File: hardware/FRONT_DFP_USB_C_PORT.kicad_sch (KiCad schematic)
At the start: 31 parts, among them J8 USB4200-03-A (VIRT FLAG MOUNT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, Q22 PMPB09R5VPX, Q23 PMPB09R5VPX, Q24 PMPB09R5VPX, Q25 PMPB09R5VPX, U13 USB5926C, U16 PTN5100BMSP

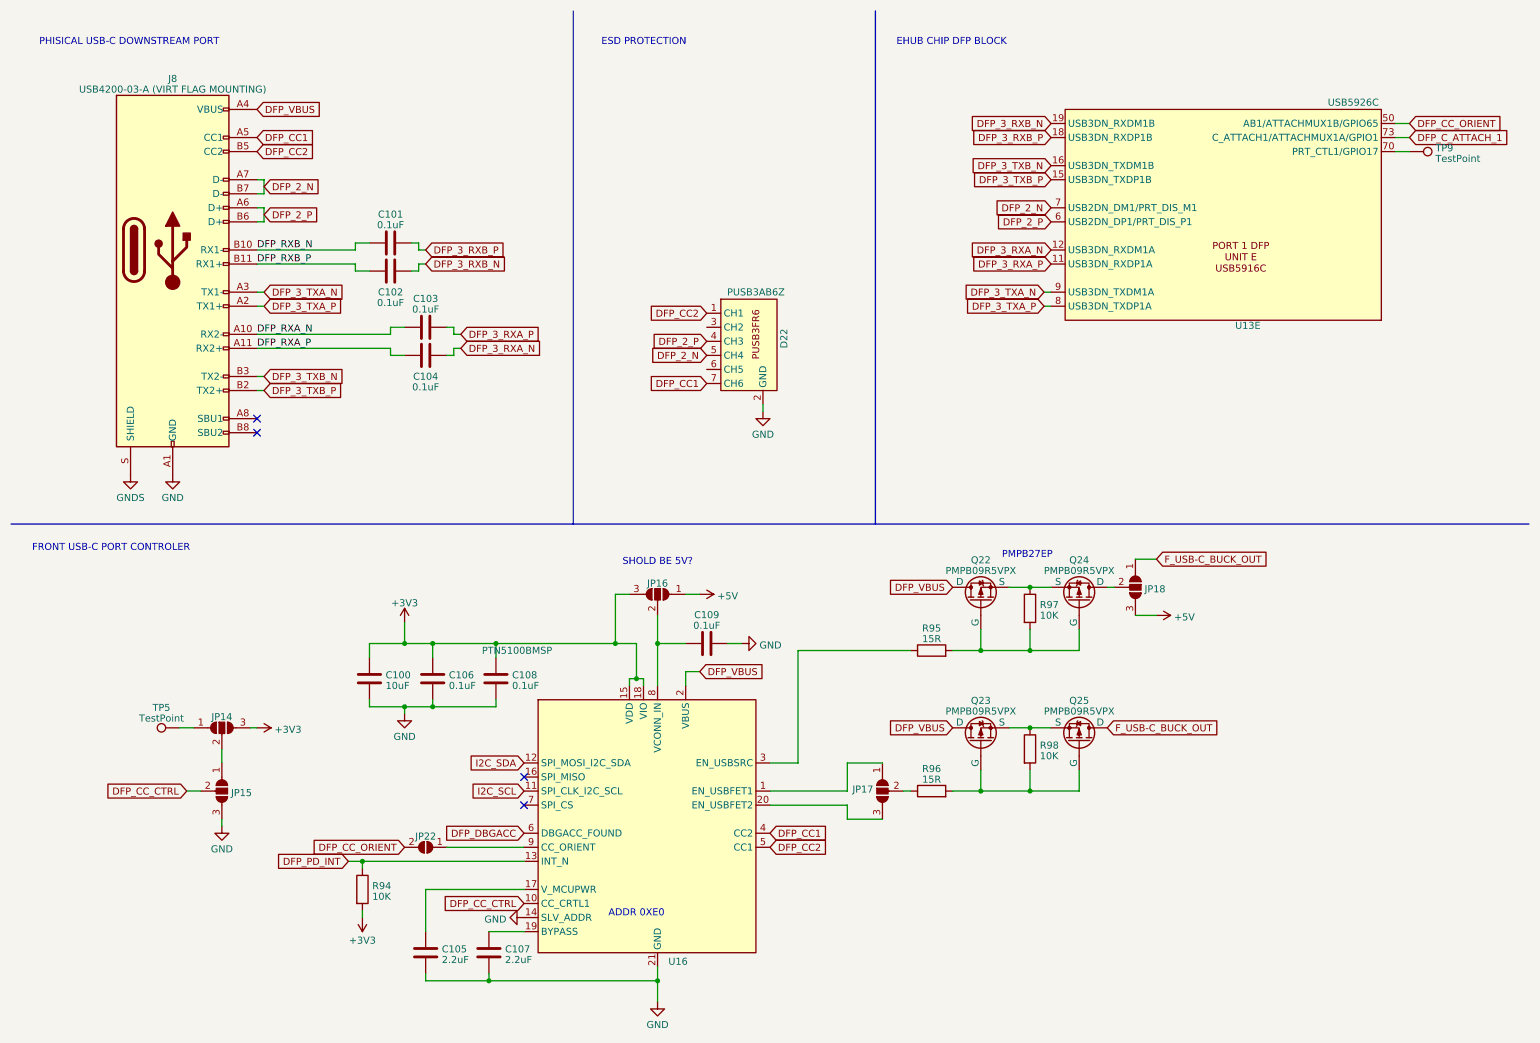
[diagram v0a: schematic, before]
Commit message: switched pd phy as old one needed an NDA
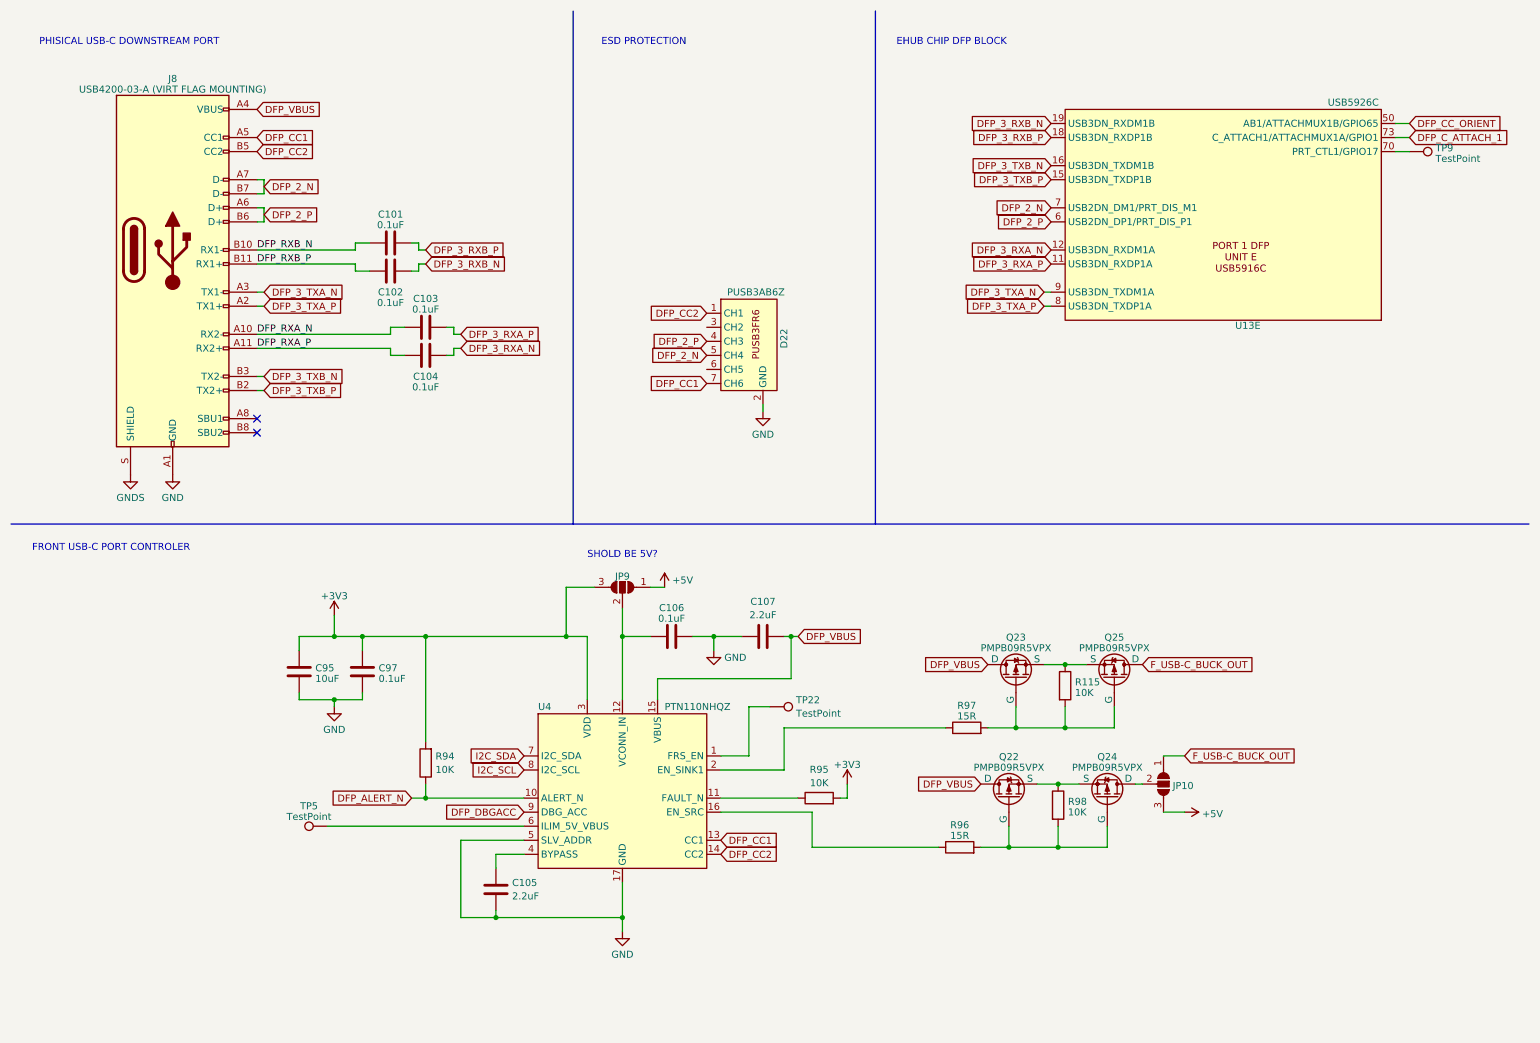
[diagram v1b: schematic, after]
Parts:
- removed C100: 10uF, Capacitor_SMD:C_0603_1608Metric, symbol Device:C
- removed C108, C109: 0.1uF, Capacitor_SMD:C_0603_1608Metric, symbol Device:C
- removed JP14, JP15, JP16, JP17, JP18: ~, Jumper:SolderJumper-3_P1.3mm_Open_RoundedPad1.0x1.5mm_NumberLabels, symbol Jumper:SolderJumper_3_Open
- removed JP22: ~, Jumper:SolderJumper-2_P1.3mm_Open_RoundedPad1.0x1.5mm, symbol Jumper:SolderJumper_2_Open
- removed U16: PTN5100BMSP, CARTHING:PTN5100BSMP, symbol CARTHING:PTN5100
- added C95: 10uF, Capacitor_SMD:C_0603_1608Metric, symbol Device:C
- added C97: 0.1uF, Capacitor_SMD:C_0603_1608Metric, symbol Device:C
- added JP10, JP9: ~, Jumper:SolderJumper-3_P1.3mm_Open_RoundedPad1.0x1.5mm_NumberLabels, symbol Jumper:SolderJumper_3_Open
- added R115: 10K, Resistor_SMD:R_0603_1608Metric, symbol Device:R
- added TP22: TestPoint, TestPoint:TestPoint_Pad_D1.5mm, symbol Connector:TestPoint
- added U4: PTN110NHQZ, CARTHING:PTN110, symbol CARTHING:PTN110
- R95: value 15R -> 10K
- R97: value 10K -> 15R
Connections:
- net +3V3: now also R95.2, C95.1, C97.1, JP9.3 (B), U4.3 (VDD); no longer C106.1
- net +5V: now also JP10.3 (B), JP9.1 (A)
- net DFP_CC1: now also U4.13 (CC1)
- net DFP_CC2: now also U4.14 (CC2)
- net DFP_DBGACC: now also U4.9 (DBG_ACC)
- net DFP_VBUS: now also C107.2, U4.15 (VBUS)
- net F_USB-C_BUCK_OUT: now also JP10.1 (A)
- net GND: now also C107.1, C95.2, C97.2, U4.17 (GND), U4.5 (SLV_ADDR); no longer C107.2
- net I2C_SCL: now also U4.8 (I2C_SCL)
- net I2C_SDA: now also U4.7 (I2C_SDA)
- net at Q23.4 (S), Q23.8 (S), Q25.4 (S)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: now also R115.1; no longer R98.1
- net at Q23.3 (G), Q25.3 (G): now also R97.2, R115.2; no longer R96.2, R98.2
- net at Q24.1 (D), Q24.2 (D), Q24.5 (D)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: now also JP10.2 (C)
- net at Q22.3 (G), Q24.3 (G): now also R96.2, R98.2; no longer R95.2, R97.2
- net at Q22.4 (S), Q22.8 (S), Q24.4 (S)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: now also R98.1; no longer R97.1
- net at R95.1: now also U4.11 (FAULT_N)
- net at R96.1: now also U4.16 (EN_SRC)
- net at C105.1: now also U4.4 (BYPASS)
- net at TP5.1: now also U4.6 (ILIM_5V_VBUS)
- net DFP_PD_INT renamed DFP_ALERT_N
- net DFP_ALERT_N: now also U4.10 (ALERT_N)
- new net: TP22.1, U4.1 (FRS_EN)
- new net: C106.1, JP9.2 (C), U4.12 (VCONN_IN)
- new net: R97.1, U4.2 (EN_SINK1)
- no-connect marks 4 -> 2
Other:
- note removed: "ADDR 0XE0"
- note removed: "PMPB27EP"

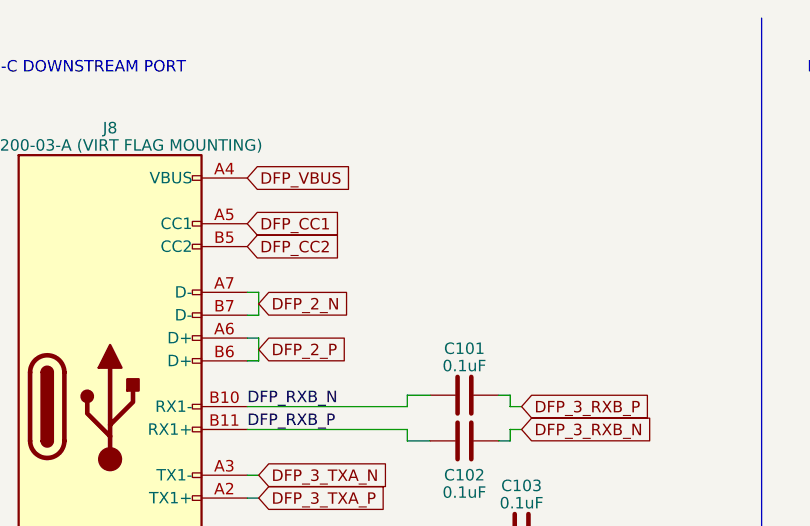
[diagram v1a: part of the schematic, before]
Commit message: updated block digram minor pcb changes
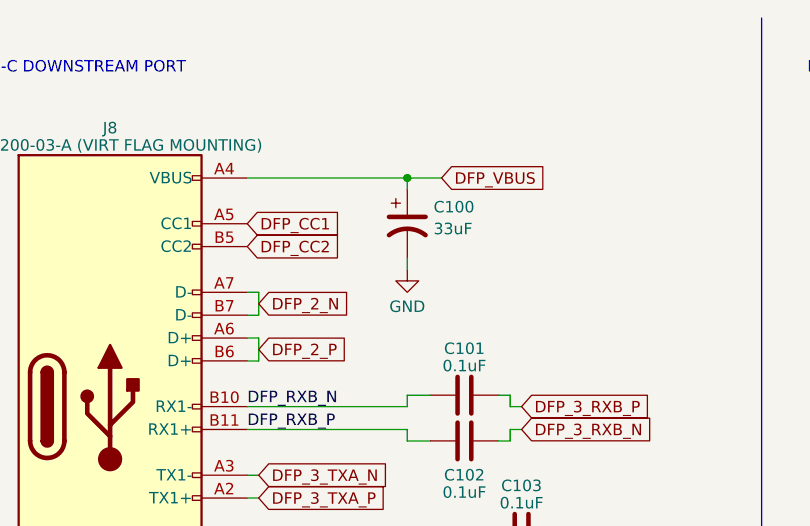
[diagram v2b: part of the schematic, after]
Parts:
- added C100: 33uF, Capacitor_SMD:C_Elec_6.3x5.8, symbol Device:C_Polarized_US
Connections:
- net DFP_VBUS: now also C100.1
- net GND: now also C100.2

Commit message: switched can tranceiver to combo controler and tranceiver
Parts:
- added TP29, TP30: TestPoint, TestPoint:TestPoint_Pad_D1.0mm, symbol Connector:TestPoint
- TP22, TP5, TP9: footprint TestPoint:TestPoint_Pad_D1.5mm -> TestPoint:TestPoint_Pad_D1.0mm
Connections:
- net at R96.1, U4.16 (EN_SRC): now also TP30.1
- net at R97.1, U4.2 (EN_SINK1): now also TP29.1
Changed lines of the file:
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@@
 	)
 	(junction
+		(at 166.37 140.97)
+		(diameter 0)
+		(color 0 0 0 0)
+	)
+	(junction
 		(at 121.92 175.26)
 		(diameter 0)
@@
 	)
 	(junction
+		(at 166.37 162.56)
+		(diameter 0)
+		(color 0 0 0 0)
+	)
+	(junction
 		(at 69.85 135.89)
 		(diameter 0)
@@
 	(wire
 		(pts
+			(xy 166.37 140.97) (xy 180.34 140.97)
+		)
+		(stroke
+			(width 0)
+			(type default)
+		)
+	)
+	(wire
+		(pts
 			(xy 99.06 173.99) (xy 99.06 175.26)
 		)
@@
 	(wire
 		(pts
-			(xy 151.13 140.97) (xy 180.34 140.97)
+			(xy 151.13 140.97) (xy 166.37 140.97)
 		)
 		(stroke
@@
 	(wire
 		(pts
+			(xy 166.37 162.56) (xy 179.07 162.56)
+		)
+		(stroke
+			(width 0)
+			(type default)
+		)
+	)
+	(wire
+		(pts
 			(xy 219.71 146.05) (xy 223.52 146.05)
 		)
@@
 	(wire
 		(pts
-			(xy 156.21 162.56) (xy 179.07 162.56)
+			(xy 156.21 162.56) (xy 166.37 162.56)
 		)
 		(stroke
@@
 			)
 		)
-		(property "Footprint" "TestPoint:TestPoint_Pad_D1.5mm"
+		(property "Footprint" "TestPoint:TestPoint_Pad_D1.0mm"
 			(at 264.16 41.91 0)
 			(effects
@@
 	)
 	(symbol
+		(lib_id "Connector:TestPoint")
+		(at 166.37 162.56 0)
+		(unit 1)
+		(exclude_from_sim no)
+		(in_bom yes)
+		(on_board yes)
+		(dnp no)
+		(fields_autoplaced yes)
+		(property "Reference" "TP30"
+			(at 167.767 158.0458 0)
+			(effects
+				(font
+					(size 1.27 1.27)
+				)
+				(justify left)
+			)
+		)
+		(property "Value" "TestPoint"
+			(at 167.767 160.4701 0)
+			(effects
+				(font
+					(size 1.27 1.27)
+				)
+				(justify left)
+			)
+		)
+		(property "Footprint" "TestPoint:TestPoint_Pad_D1.0mm"
+			(at 171.45 162.56 0)
+			(effects
+				(font
+					(size 1.27 1.27)
+				)
+				(hide yes)
+			)
+		)
+		(property "Datasheet" "~"
+			(at 171.45 162.56 0)
+			(effects
+				(font
+					(size 1.27 1.27)
+				)
+				(hide yes)
+			)
+		)
+		(property "Description" "test point"
+			(at 166.37 162.56 0)
+			(effects
+				(font
+					(size 1.27 1.27)
+				)
+				(hide yes)
+			)
+		)
+		(pin "1"
+		)
+		(instances
+			(project "usbc-car-module"
+				(path "/fae025e9-99c5-40c1-af6f-99dc1edbfa43/ad0dde3f-c33d-40ce-8876-17a95cda421b"
+					(reference "TP30")
+					(unit 1)
+				)
+			)
+		)
+	)
+	(symbol
 		(lib_id "Device:C")
 		(at 74.93 130.81 0)
@@
 			)
 		)
-		(property "Footprint" "TestPoint:TestPoint_Pad_D1.5mm"
+		(property "Footprint" "TestPoint:TestPoint_Pad_D1.0mm"
 			(at 68.58 153.67 0)
 			(effects
@@
 			)
 		)
-		(property "Footprint" "TestPoint:TestPoint_Pad_D1.5mm"
+		(property "Footprint" "TestPoint:TestPoint_Pad_D1.0mm"
 			(at 148.59 142.24 0)
 			(effects
@@
 					(unit 1)
 				)
+			)
+		)
+	)
+	(symbol
+		(lib_id "Connector:TestPoint")
+		(at 166.37 140.97 0)
+		(unit 1)
+		(exclude_from_sim no)
+		(in_bom yes)
+		(on_board yes)
+		(dnp no)
+		(fields_autoplaced yes)
+		(property "Reference" "TP29"
+			(at 167.767 136.4558 0)
+			(effects
+				(font
+					(size 1.27 1.27)
+				)
+				(justify left)
+			)
+		)
+		(property "Value" "TestPoint"
+			(at 167.767 138.8801 0)
+			(effects
+				(font
+					(size 1.27 1.27)
+				)
+				(justify left)
+			)
+		)
+		(property "Footprint" "TestPoint:TestPoint_Pad_D1.0mm"
+			(at 171.45 140.97 0)
+			(effects
+				(font
+					(size 1.27 1.27)
+				)
+				(hide yes)
+			)
+		)
+		(property "Datasheet" "~"
+			(at 171.45 140.97 0)
+			(effects
+				(font
+					(size 1.27 1.27)
+				)
+				(hide yes)
+			)
+		)
+		(property "Description" "test point"
+			(at 166.37 140.97 0)
+			(effects
+				(font
+					(size 1.27 1.27)
+				)
+				(hide yes)
+			)
+		)
+		(pin "1"
+		)
+		(instances
+			(project "usbc-car-module"
+				(path "/fae025e9-99c5-40c1-af6f-99dc1edbfa43/ad0dde3f-c33d-40ce-8876-17a95cda421b"
+					(reference "TP29")
+					(unit 1)
+				)

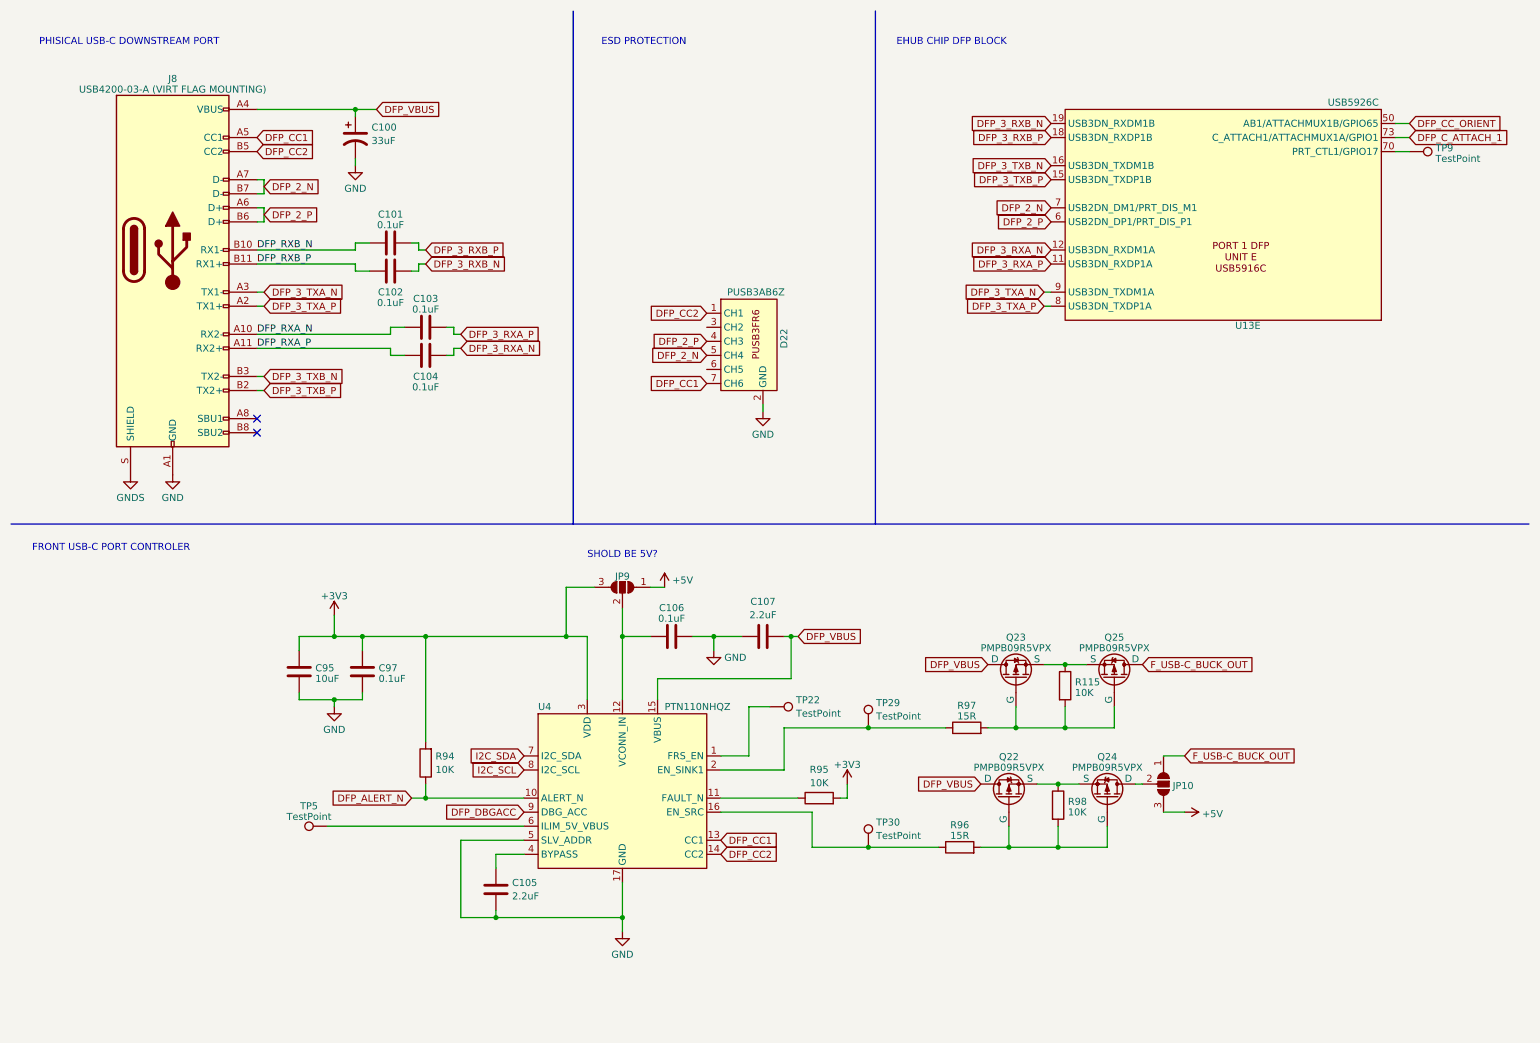
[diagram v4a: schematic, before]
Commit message: migrated to the esp32-s2 and starting new board revison
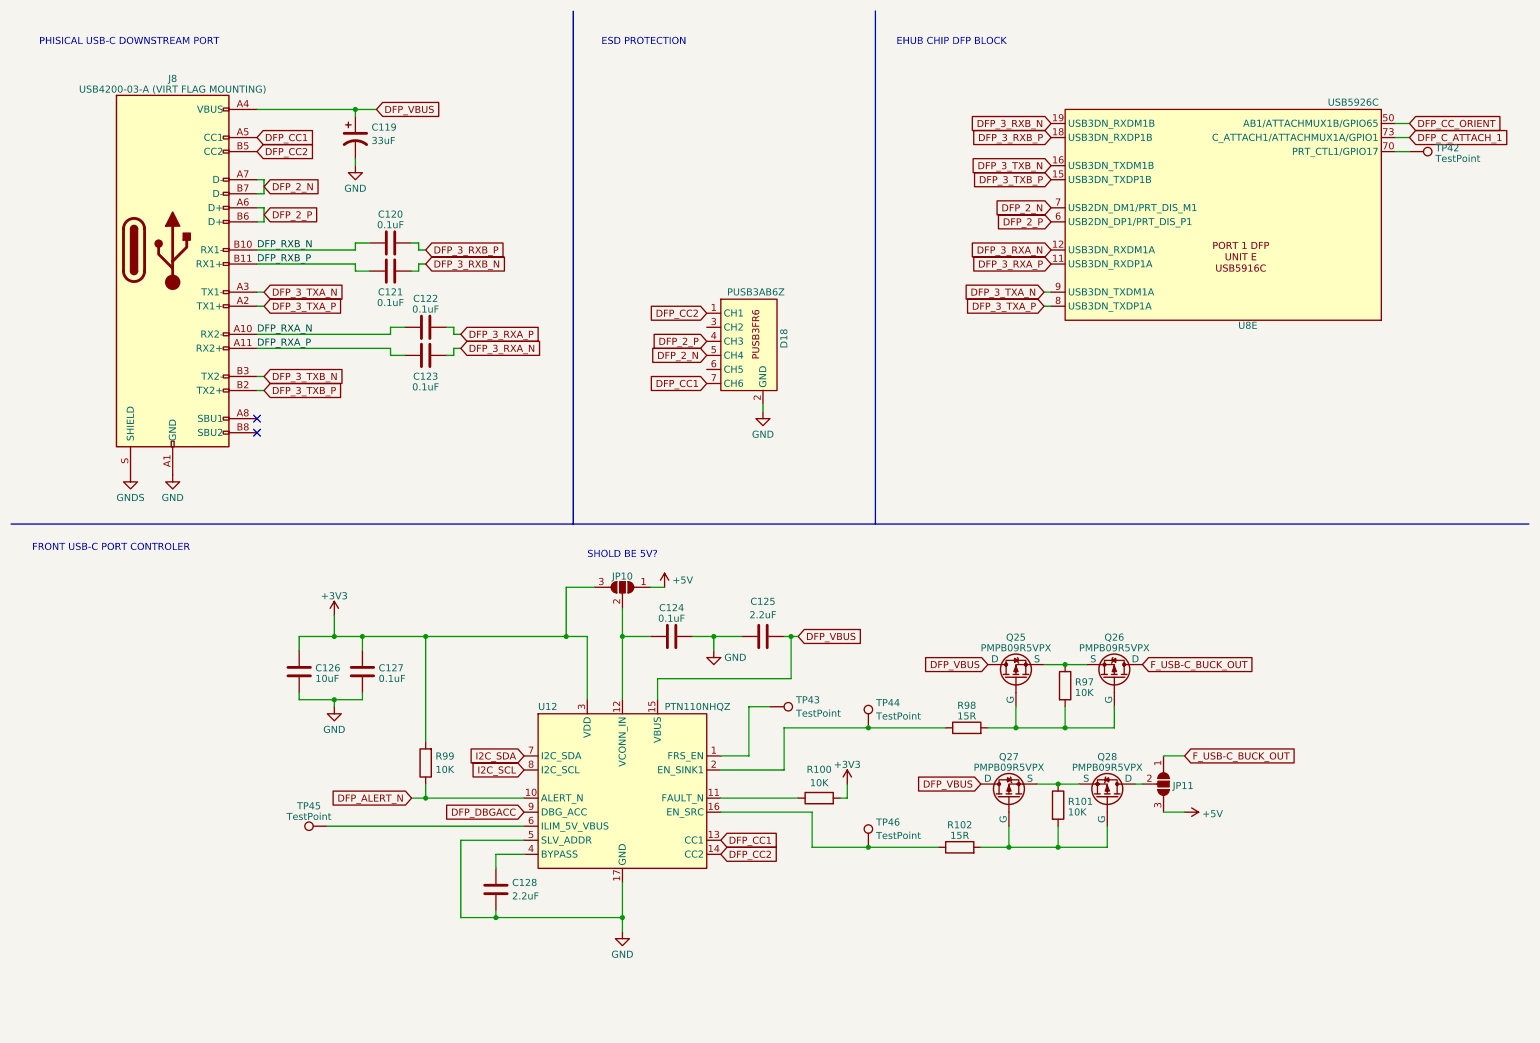
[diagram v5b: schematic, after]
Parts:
- renumbered C100 to C119, C101 to C120, C102 to C121, C103 to C122, C104 to C123, C106 to C124, C107 to C125, C95 to C126, C97 to C127, C105 to C128, D22 to D18, JP9 to JP10, JP10 to JP11, Q23 to Q25, Q25 to Q26, Q22 to Q27, Q24 to Q28, R95 to R100, R98 to R101, R96 to R102, R115 to R97, R97 to R98, R94 to R99, TP9 to TP42, TP22 to TP43, TP29 to TP44, TP5 to TP45, TP30 to TP46, U4 to U12, U13 to U8
